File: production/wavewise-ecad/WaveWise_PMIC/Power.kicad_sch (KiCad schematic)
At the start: 24 parts, among them IC1 LV14360PDDAR, U1 LM2576HVS-5.0_NOPB, U2 LM2576HVS-12.0_NOPB

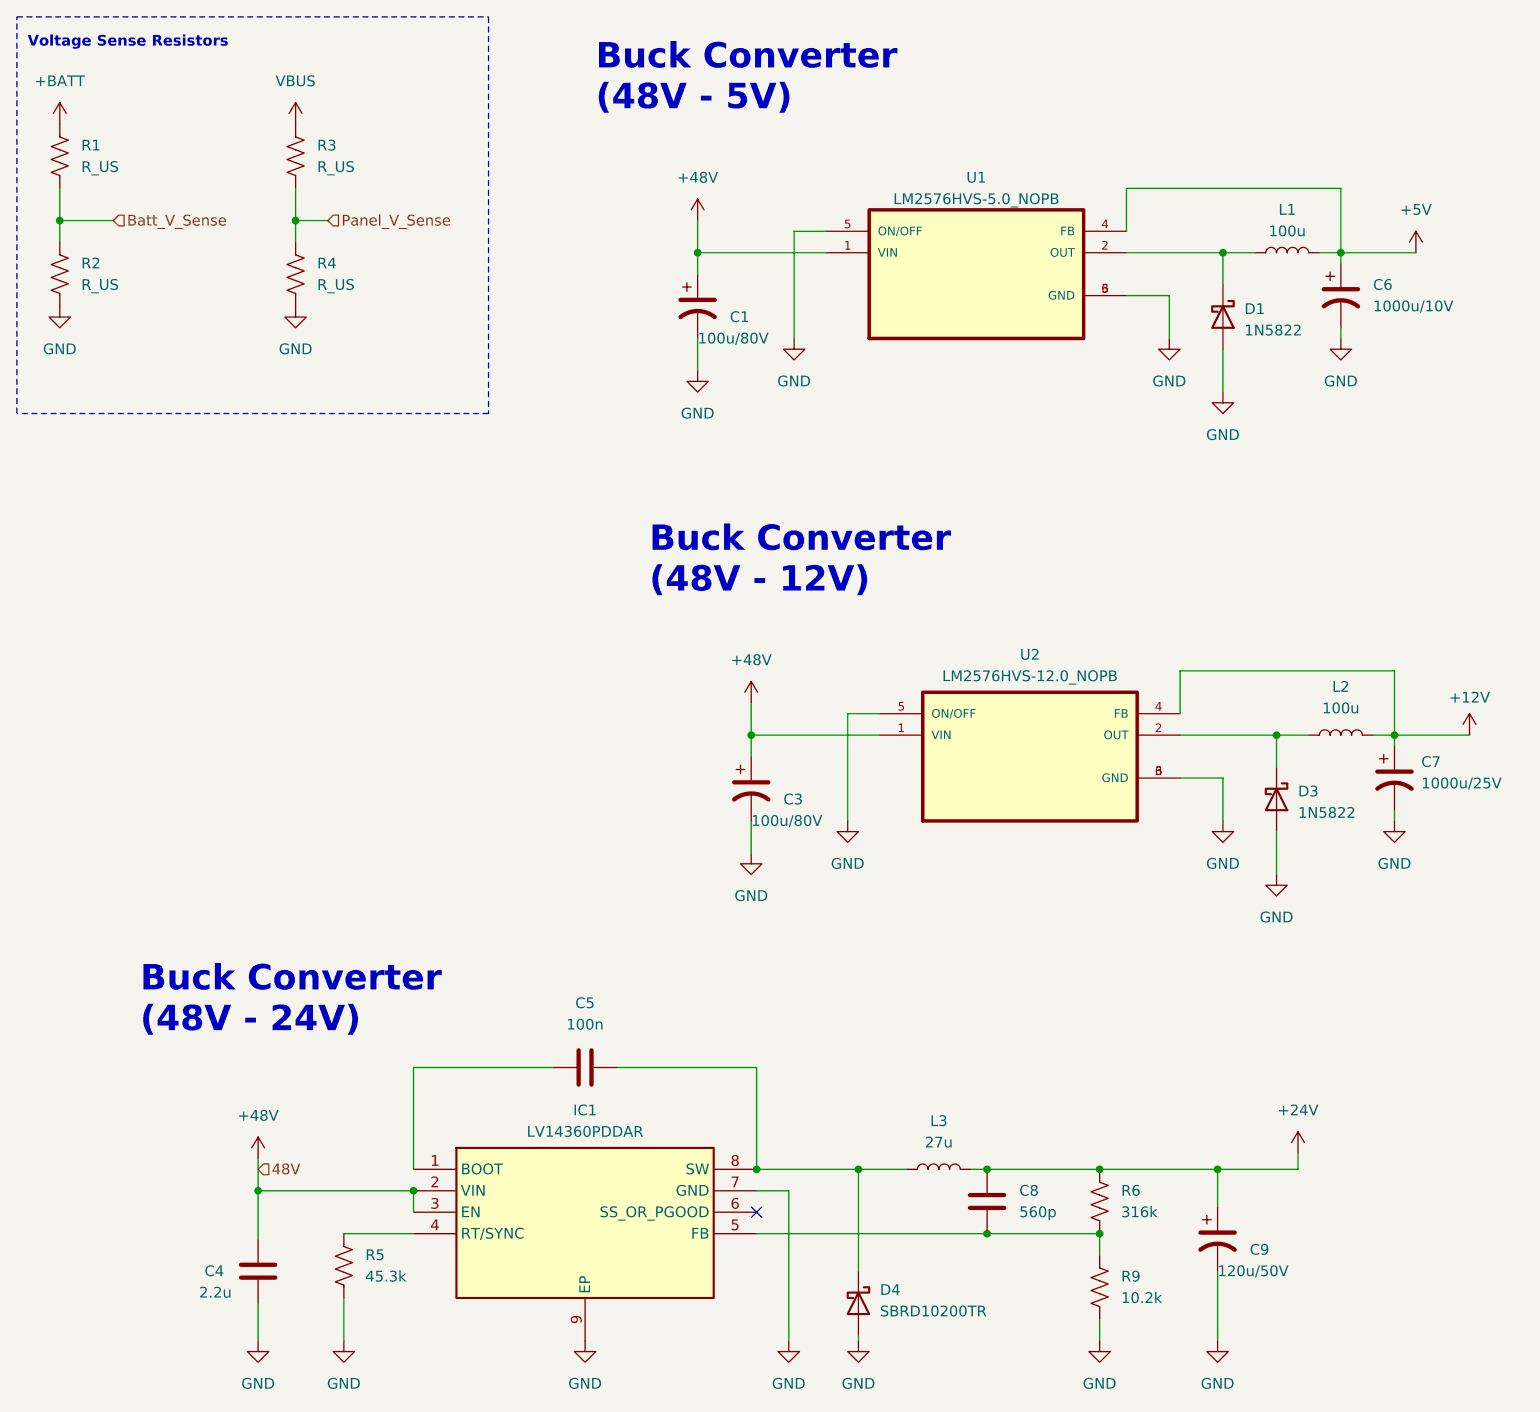
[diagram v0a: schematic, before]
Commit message: Added some footprints not all yet though
Footprint addition 3/14/2024
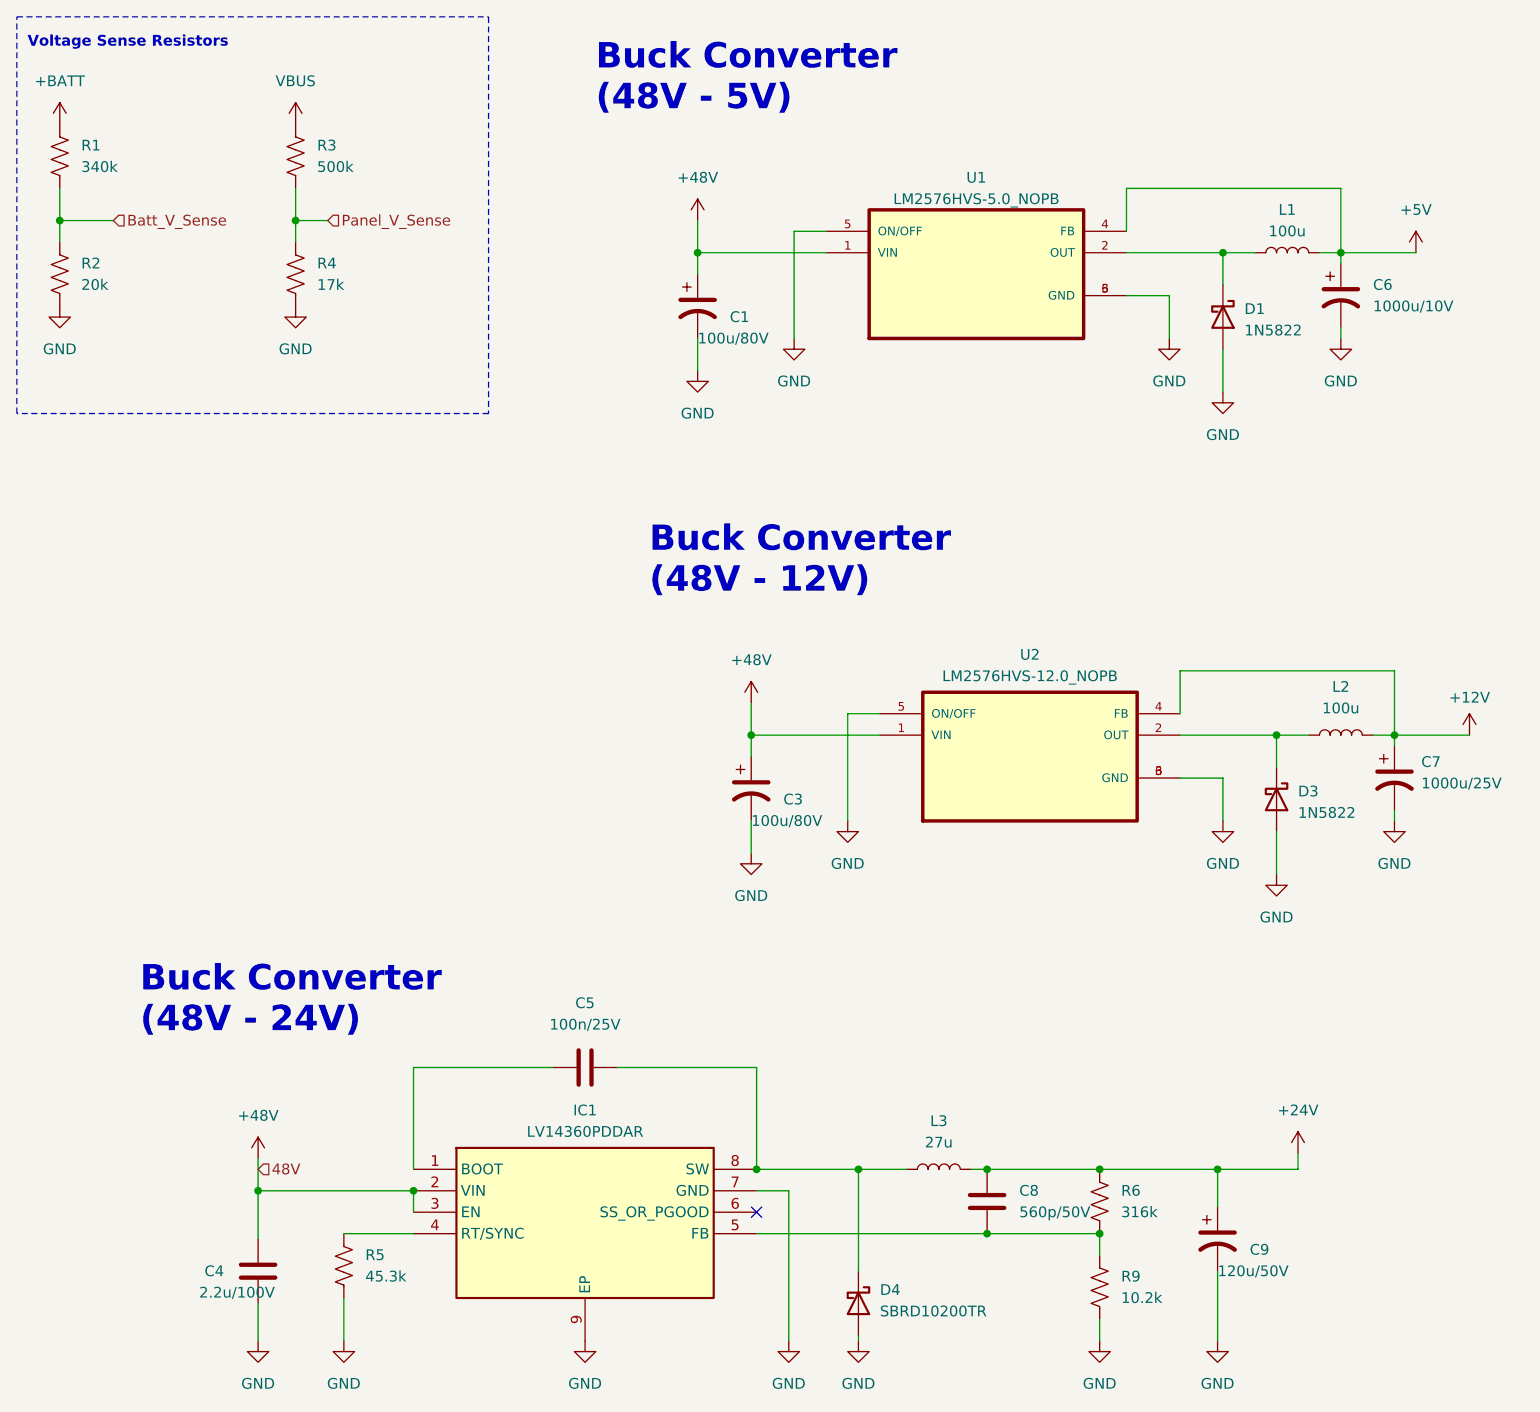
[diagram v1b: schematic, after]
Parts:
- C1, C3: footprint Wavewise Footprints UnChecked:100uF_80V_Cap -> Capacitor_SMD:C_1206_3216Metric_Pad1.33x1.80mm_HandSolder
- C4: value 2.2u -> 2.2u/100V; footprint (none) -> Capacitor_SMD:C_1210_3225Metric_Pad1.33x2.70mm_HandSolder
- C5: value 100n -> 100n/25V; footprint (none) -> Capacitor_SMD:C_0402_1005Metric_Pad0.74x0.62mm_HandSolder
- C8: value 560p -> 560p/50V; footprint (none) -> Capacitor_SMD:C_0805_2012Metric_Pad1.18x1.45mm_HandSolder
- L1, L2, L3: footprint Wavewise Footprints UnChecked:IND_ETQP5M101YGK -> Inductor_SMD:L_12x12mm_H6mm
- R1: value R_US -> 340k
- R2: value R_US -> 20k
- R3: value R_US -> 500k
- R4: value R_US -> 17k
- R5, R6: footprint (none) -> Resistor_SMD:R_0805_2012Metric_Pad1.20x1.40mm_HandSolder
- U1, U2: footprint Wavewise Footprints UnChecked:LM2576S-12_NOPB -> Package_TO_SOT_SMD:TO-263-5_TabPin3
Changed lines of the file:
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@@
       (effects (font (size 1.27 1.27)) (justify left))
     )
-    (property "Footprint" "" (at 52.451 160.909 90)
+    (property "Footprint" "Resistor_SMD:R_0805_2012Metric_Pad1.20x1.40mm_HandSolder" (at 52.451 160.909 90)
       (effects (font (size 1.27 1.27)) hide)
     )
@@
       (effects (font (size 1.27 1.27)))
     )
-    (property "Footprint" "Wavewise Footprints UnChecked:LM2576S-12_NOPB" (at 126.365 43.18 0)
+    (property "Footprint" "Package_TO_SOT_SMD:TO-263-5_TabPin3" (at 126.365 43.18 0)
       (effects (font (size 1.27 1.27)) (justify bottom) hide)
     )
@@
       (effects (font (size 1.27 1.27)))
     )
-    (property "Footprint" "Wavewise Footprints UnChecked:IND_ETQP5M101YGK" (at 163.195 40.64 0)
+    (property "Footprint" "Inductor_SMD:L_12x12mm_H6mm" (at 163.195 40.64 0)
       (effects (font (size 1.27 1.27)) hide)
     )
@@
       (effects (font (size 1.27 1.27)))
     )
-    (property "Footprint" "Wavewise Footprints UnChecked:IND_ETQP5M101YGK" (at 121.92 149.225 0)
+    (property "Footprint" "Inductor_SMD:L_12x12mm_H6mm" (at 121.92 149.225 0)
       (effects (font (size 1.27 1.27)) hide)
     )
@@
       (effects (font (size 1.27 1.27)) (justify left))
     )
-    (property "Footprint" "Wavewise Footprints UnChecked:100uF_80V_Cap" (at 93.345 46.99 0)
+    (property "Footprint" "Capacitor_SMD:C_1206_3216Metric_Pad1.33x1.80mm_HandSolder" (at 93.345 46.99 0)
       (effects (font (size 1.27 1.27)) hide)
     )
@@
       (effects (font (size 1.27 1.27)) (justify left))
     )
-    (property "Footprint" "Wavewise Footprints UnChecked:100uF_80V_Cap" (at 99.695 104.14 0)
+    (property "Footprint" "Capacitor_SMD:C_1206_3216Metric_Pad1.33x1.80mm_HandSolder" (at 99.695 104.14 0)
       (effects (font (size 1.27 1.27)) hide)
     )
@@
       (effects (font (size 1.27 1.27)) (justify right))
     )
-    (property "Value" "560p" (at 131.445 154.305 0)
+    (property "Value" "560p/50V" (at 131.445 154.305 0)
       (effects (font (size 1.27 1.27)) (justify right))
     )
-    (property "Footprint" "" (at 126.6698 149.225 0)
+    (property "Footprint" "Capacitor_SMD:C_0805_2012Metric_Pad1.18x1.45mm_HandSolder" (at 126.6698 149.225 0)
       (effects (font (size 1.27 1.27)) hide)
     )
@@
       (effects (font (size 1.27 1.27)))
     )
-    (property "Footprint" "Wavewise Footprints UnChecked:IND_ETQP5M101YGK" (at 169.545 97.79 0)
+    (property "Footprint" "Inductor_SMD:L_12x12mm_H6mm" (at 169.545 97.79 0)
       (effects (font (size 1.27 1.27)) hide)
     )
@@
       (effects (font (size 1.27 1.27)))
     )
-    (property "Value" "100n" (at 80.01 132.08 90)
-      (effects (font (size 1.27 1.27)))
-    )
-    (property "Footprint" "" (at 83.82 136.1948 0)
+    (property "Value" "100n/25V" (at 80.01 132.08 90)
+      (effects (font (size 1.27 1.27)))
+    )
+    (property "Footprint" "Capacitor_SMD:C_0402_1005Metric_Pad0.74x0.62mm_HandSolder" (at 83.82 136.1948 0)
       (effects (font (size 1.27 1.27)) hide)
     )
@@
       (effects (font (size 1.27 1.27)) (justify left))
     )
-    (property "Value" "R_US" (at 20.32 30.48 0)
+    (property "Value" "340k" (at 20.32 30.48 0)
       (effects (font (size 1.27 1.27)) (justify left))
     )
@@
       (effects (font (size 1.27 1.27)))
     )
-    (property "Footprint" "Wavewise Footprints UnChecked:LM2576S-12_NOPB" (at 132.715 100.33 0)
+    (property "Footprint" "Package_TO_SOT_SMD:TO-263-5_TabPin3" (at 132.715 100.33 0)
       (effects (font (size 1.27 1.27)) (justify bottom) hide)
     )
@@
       (effects (font (size 1.27 1.27)) (justify left))
     )
-    (property "Footprint" "" (at 141.986 153.289 90)
+    (property "Footprint" "Resistor_SMD:R_0805_2012Metric_Pad1.20x1.40mm_HandSolder" (at 141.986 153.289 90)
       (effects (font (size 1.27 1.27)) hide)
     )
@@
       (effects (font (size 1.27 1.27)) (justify left))
     )
-    (property "Value" "R_US" (at 48.26 30.48 0)
+    (property "Value" "500k" (at 48.26 30.48 0)
       (effects (font (size 1.27 1.27)) (justify left))
     )
@@
       (effects (font (size 1.27 1.27)) (justify left))
     )
-    (property "Value" "R_US" (at 48.26 44.45 0)
+    (property "Value" "17k" (at 48.26 44.45 0)
       (effects (font (size 1.27 1.27)) (justify left))
     )
@@
       (effects (font (size 1.27 1.27)) (justify left))
     )
-    (property "Value" "2.2u" (at 34.29 163.83 0)
-      (effects (font (size 1.27 1.27)) (justify left))
-    )
-    (property "Footprint" "" (at 42.2402 165.1 0)
+    (property "Value" "2.2u/100V" (at 34.29 163.83 0)
+      (effects (font (size 1.27 1.27)) (justify left))
+    )
+    (property "Footprint" "Capacitor_SMD:C_1210_3225Metric_Pad1.33x2.70mm_HandSolder" (at 42.2402 165.1 0)
       (effects (font (size 1.27 1.27)) hide)
     )
@@
       (effects (font (size 1.27 1.27)) (justify left))
     )
-    (property "Value" "R_US" (at 20.32 44.45 0)
-      (effects (font (size 1.27 1.27)) (justify left))
-    )
+    (property "Value" "20k" (at 20.32 44.45 0)
+      (effects (font (size 1.27 1.27)) (justify left))
+    )
